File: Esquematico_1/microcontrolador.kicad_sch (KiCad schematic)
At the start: 31 parts, among them U2 STM32F405RGTx, Y1 Crystal

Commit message: Cristales y arreglo de los simbolos que no estaban en referencia
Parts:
- removed Y1: Crystal, symbol Device:Crystal
- added Y1: ABMM-8.000MHZ-D-4-T, ABMM25000MHZB2T, symbol ABMM-8_000MHZ-D-4-T:ABMM-8.000MHZ-D-4-T
- C5: value 10u -> 16pF
- C6: value C -> 16pF
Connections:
- net GND: now also C5.2, Y1.2 (METAL_LID_1), Y1.4 (METAL_LID_2); no longer C5.1
- net HSE_IN: now reaches U2.5 (PH0)
- net HSE_IN: now also C6.1, Y1.1 (X1); no longer C5.2
- net HSE_OUT: now reaches U2.6 (PH1)
- net HSE_OUT: now also C5.1, Y1.3 (X2); no longer C6.1
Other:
- moved on the sheet: C20, C21, C22, C23, C24, C25, C26, C27, C28, C29, C30, C31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

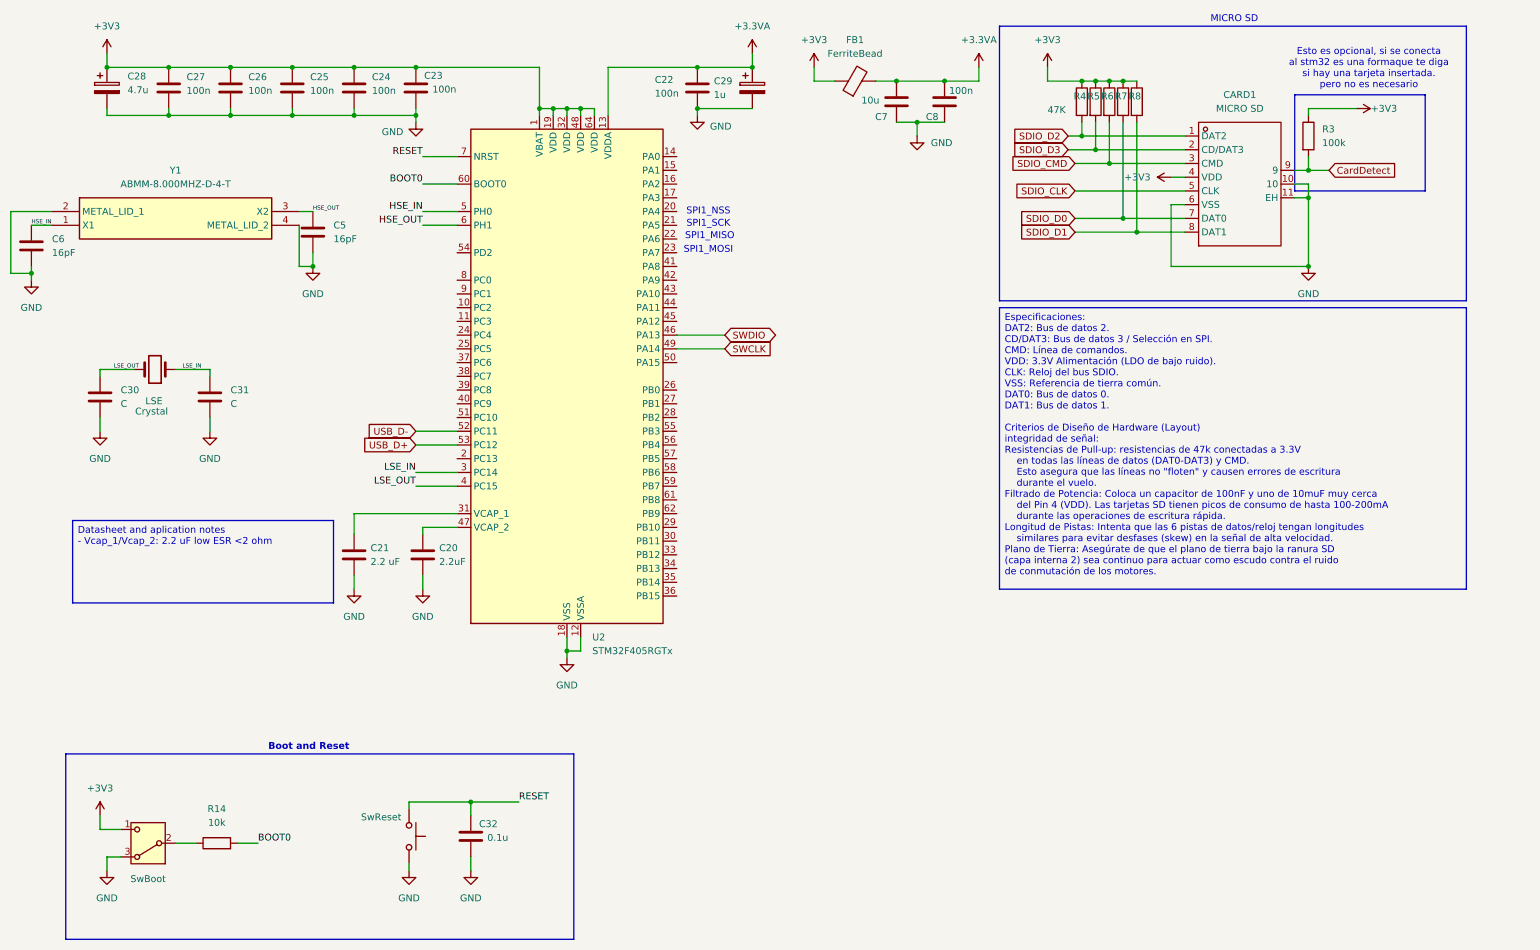
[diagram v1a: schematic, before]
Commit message: Conexiones con MCU, IMU, VTX, ELRS y  Magnometro
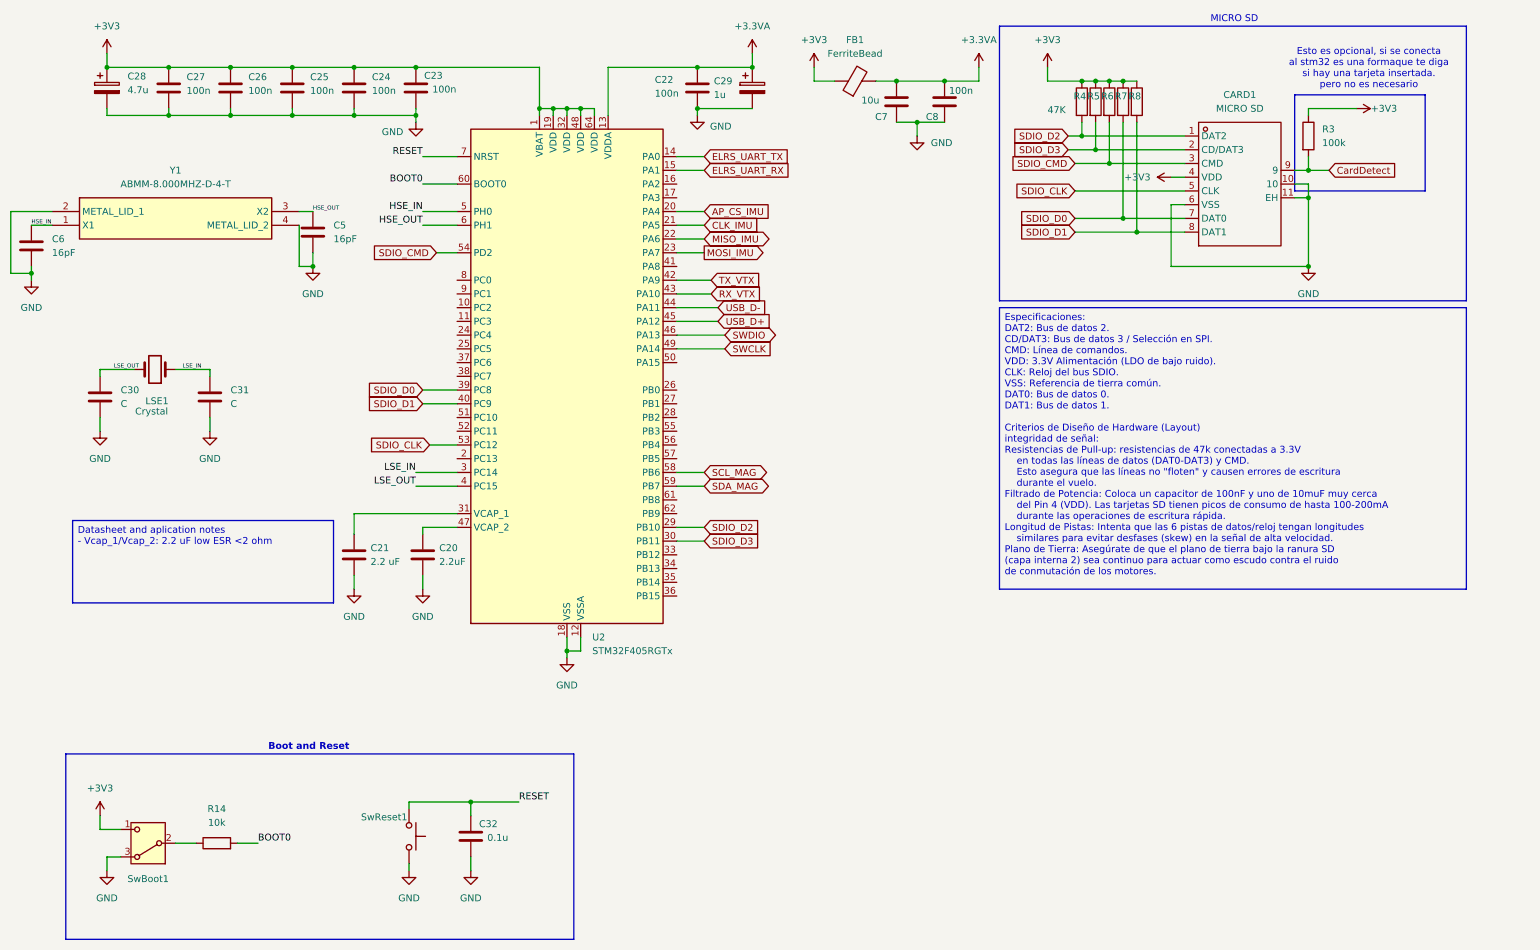
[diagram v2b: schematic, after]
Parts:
- Y1: footprint ABMM25000MHZB2T -> ABMM-8.000MHZ-D-4-T:ABMM25000MHZB2T
- renumbered LSE to LSE1, SwBoot to SwBoot1, SwReset to SwReset1
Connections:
- net SDIO_CLK: now also U2.53 (PC12)
- net SDIO_CMD: now also U2.54 (PD2)
- net SDIO_D0: now also U2.39 (PC8)
- net SDIO_D1: now also U2.40 (PC9)
- net SDIO_D2: now also U2.29 (PB10)
- net SDIO_D3: now also U2.30 (PB11)
- net USB_D+: now also U2.45 (PA12); no longer U2.53 (PC12)
- net USB_D-: now also U2.44 (PA11); no longer U2.52 (PC11)
- net ELRS_UART_TX: now reaches U2.14 (PA0)
- net ELRS_UART_RX: now reaches U2.15 (PA1)
- net AP_CS_IMU: now reaches U2.20 (PA4)
- net CLK_IMU: now reaches U2.21 (PA5)
- net MISO_IMU: now reaches U2.22 (PA6)
- net MOSI_IMU: now reaches U2.23 (PA7)
- net TX_VTX: now reaches U2.42 (PA9)
- net RX_VTX: now reaches U2.43 (PA10)
- net SCL_MAG: now reaches U2.58 (PB6)
- net SDA_MAG: now reaches U2.59 (PB7)
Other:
- note removed: "SPI1_MISO"
- note removed: "SPI1_MOSI"
- note removed: "SPI1_NSS"
- note removed: "SPI1_SCK"

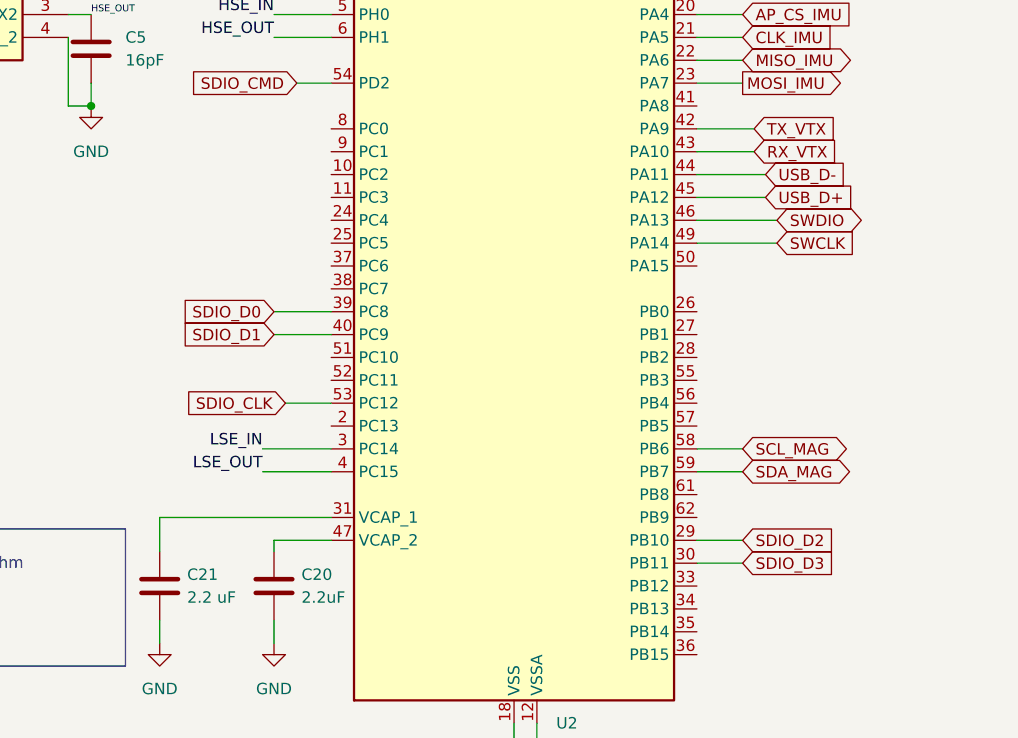
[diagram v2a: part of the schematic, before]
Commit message: último sensor conectado, y le quité los colores al net_signal xdd
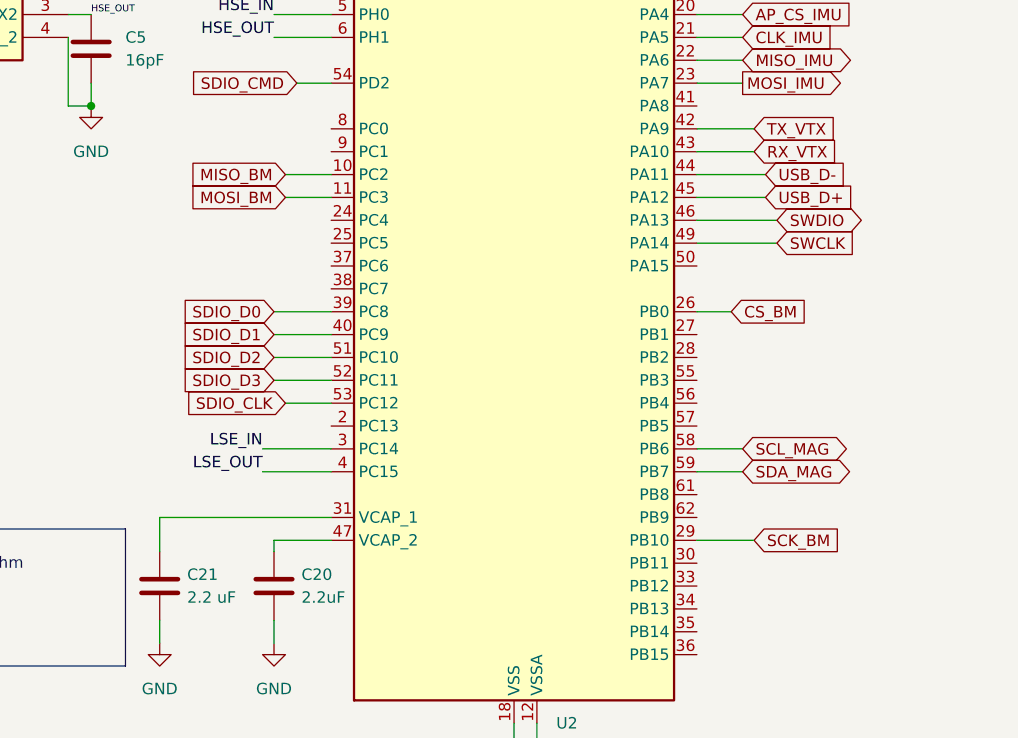
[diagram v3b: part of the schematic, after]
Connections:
- net SDIO_D2: now also U2.51 (PC10); no longer U2.29 (PB10)
- net SDIO_D3: now also U2.52 (PC11); no longer U2.30 (PB11)
- net MISO_BM: now reaches U2.10 (PC2)
- net MOSI_BM: now reaches U2.11 (PC3)
- net CS_BM: now reaches U2.26 (PB0)
- new net SCK_BM: U2.29 (PB10)
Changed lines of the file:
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@@
-	(wire
-		(pts
-			(xy 135.89 110.49) (xy 140.97 110.49)
-		)
-		(stroke
-			(width 0)
-			(type default)
-		)
-	)
 	(wire
 		(pts
@@
 	(wire
 		(pts
+			(xy 90.17 69.85) (xy 95.25 69.85)
+		)
+		(stroke
+			(width 0)
+			(type default)
+		)
+	)
+	(wire
+		(pts
+			(xy 95.25 90.17) (xy 88.9 90.17)
+		)
+		(stroke
+			(width 0)
+			(type default)
+		)
+	)
+	(wire
+		(pts
 			(xy 90.17 95.25) (xy 95.25 95.25)
 		)
@@
 	(wire
 		(pts
+			(xy 142.24 110.49) (xy 135.89 110.49)
+		)
+		(stroke
+			(width 0)
+			(type default)
+		)
+	)
+	(wire
+		(pts
 			(xy 135.89 77.47) (xy 144.78 77.47)
 		)
@@
 	(wire
 		(pts
+			(xy 88.9 92.71) (xy 95.25 92.71)
+		)
+		(stroke
+			(width 0)
+			(type default)
+		)
+	)
+	(wire
+		(pts
 			(xy 118.11 133.35) (xy 115.57 133.35)
 		)
@@
 	(wire
 		(pts
-			(xy 140.97 113.03) (xy 135.89 113.03)
-		)
-		(stroke
-			(width 0)
-			(type default)
-		)
-	)
-	(wire
-		(pts
 			(xy 53.34 25.4) (xy 64.77 25.4)
 		)
@@
 	(wire
 		(pts
+			(xy 90.17 72.39) (xy 95.25 72.39)
+		)
+		(stroke
+			(width 0)
+			(type default)
+		)
+	)
+	(wire
+		(pts
 			(xy 252.73 49.53) (xy 252.73 62.23)
 		)
@@
 		(pts
 			(xy 115.57 133.35) (xy 115.57 134.62)
+		)
+		(stroke
+			(width 0)
+			(type default)
+		)
+	)
+	(wire
+		(pts
+			(xy 139.7 85.09) (xy 135.89 85.09)
 		)
 		(stroke
@@
 			)
 			(justify right bottom)
+		)
+	)
+	(global_label "SCK_BM"
+		(shape input)
+		(at 142.24 110.49 0)
+		(fields_autoplaced yes)
+		(effects
+			(font
+				(size 1.27 1.27)
+			)
+			(justify left)
+		)
+		(property "Intersheetrefs" "${INTERSHEET_REFS}"
+			(at 152.6637 110.49 0)
+			(effects
+				(font
+					(size 1.27 1.27)
+				)
+				(justify left)
+				(hide yes)
+			)
 		)
 	)
@@
 		)
 	)
-	(global_label "SDIO_D2"
-		(shape input)
-		(at 140.97 110.49 0)
-		(fields_autoplaced yes)
-		(effects
-			(font
-				(size 1.27 1.27)
+	(global_label "TX_VTX"
+		(shape input)
+		(at 142.24 64.77 0)
+		(fields_autoplaced yes)
+		(effects
+			(font
+				(size 1.27 1.27)
+				(thickness 0.1588)
 			)
 			(justify left)
 		)
 		(property "Intersheetrefs" "${INTERSHEET_REFS}"
-			(at 151.8171 110.49 0)
+			(at 151.6356 64.77 0)
 			(effects
 				(font
@@
 		)
 	)
-	(global_label "TX_VTX"
-		(shape input)
-		(at 142.24 64.77 0)
-		(fields_autoplaced yes)
-		(effects
-			(font
-				(size 1.27 1.27)
-				(thickness 0.1588)
+	(global_label "SDIO_D0"
+		(shape input)
+		(at 88.9 85.09 180)
+		(fields_autoplaced yes)
+		(effects
+			(font
+				(size 1.27 1.27)
+			)
+			(justify right)
+		)
+		(property "Intersheetrefs" "${INTERSHEET_REFS}"
+			(at 78.0529 85.09 0)
+			(effects
+				(font
+					(size 1.27 1.27)
+				)
+				(justify right)
+				(hide yes)
+			)
+		)
+	)
+	(global_label "SDIO_D0"
+		(shape input)
+		(at 209.55 53.34 180)
+		(fields_autoplaced yes)
+		(effects
+			(font
+				(size 1.27 1.27)
+			)
+			(justify right)
+		)
+		(property "Intersheetrefs" "${INTERSHEET_REFS}"
+			(at 198.7029 53.34 0)
+			(effects
+				(font
+					(size 1.27 1.27)
+				)
+				(justify right)
+				(hide yes)
+			)
+		)
+	)
+	(global_label "AP_CS_IMU"
+		(shape input)
+		(at 140.97 52.07 0)
+		(fields_autoplaced yes)
+		(effects
+			(font
+				(size 1.27 1.27)
 			)
 			(justify left)
 		)
 		(property "Intersheetrefs" "${INTERSHEET_REFS}"
-			(at 151.6356 64.77 0)
+			(at 154.1152 52.07 0)
 			(effects
 				(font
@@
 		)
 	)
-	(global_label "SDIO_D0"
-		(shape input)
-		(at 88.9 85.09 180)
+	(global_label "SDIO_CMD"
+		(shape input)
+		(at 91.44 59.69 180)
 		(fields_autoplaced yes)
 		(effects
@@
 		)
 		(property "Intersheetrefs" "${INTERSHEET_REFS}"
-			(at 78.0529 85.09 0)
+			(at 79.081 59.69 0)
 			(effects
 				(font
@@
 		)
 	)
-	(global_label "SDIO_D0"
-		(shape input)
-		(at 209.55 53.34 180)
-		(fields_autoplaced yes)
-		(effects
-			(font
-				(size 1.27 1.27)
-			)
-			(justify right)
-		)
-		(property "Intersheetrefs" "${INTERSHEET_REFS}"
-			(at 198.7029 53.34 0)
-			(effects
-				(font
-					(size 1.27 1.27)
-				)
-				(justify right)
-				(hide yes)
-			)
-		)
-	)
-	(global_label "AP_CS_IMU"
-		(shape input)
-		(at 140.97 52.07 0)
+	(global_label "CS_BM"
+		(shape input)
+		(at 139.7 85.09 0)
 		(fields_autoplaced yes)
 		(effects
@@
 		)
 		(property "Intersheetrefs" "${INTERSHEET_REFS}"
-			(at 154.1152 52.07 0)
-			(effects
-				(font
-					(size 1.27 1.27)
-				)
-				(justify left)
-				(hide yes)
-			)
-		)
-	)
-	(global_label "SDIO_CMD"
-		(shape input)
-		(at 91.44 59.69 180)
-		(fields_autoplaced yes)
-		(effects
-			(font
-				(size 1.27 1.27)
-			)
-			(justify right)
-		)
-		(property "Intersheetrefs" "${INTERSHEET_REFS}"
-			(at 79.081 59.69 0)
-			(effects
-				(font
-					(size 1.27 1.27)
-				)
-				(justify right)
-				(hide yes)
-			)
-		)
-	)
-	(global_label "SDIO_D3"
-		(shape input)
-		(at 140.97 113.03 0)
-		(fields_autoplaced yes)
-		(effects
-			(font
-				(size 1.27 1.27)
-			)
-			(justify left)
-		)
-		(property "Intersheetrefs" "${INTERSHEET_REFS}"
-			(at 151.8171 113.03 0)
+			(at 148.8537 85.09 0)
 			(effects
 				(font
@@
 	(global_label "SDIO_D3"
 		(shape input)
+		(at 88.9 92.71 180)
+		(fields_autoplaced yes)
+		(effects
+			(font
+				(size 1.27 1.27)
+			)
+			(justify right)
+		)
+		(property "Intersheetrefs" "${INTERSHEET_REFS}"
+			(at 78.0529 92.71 0)
+			(effects
+				(font
+					(size 1.27 1.27)
+				)
+				(justify right)
+				(hide yes)
+			)
+		)
+	)
+	(global_label "SDIO_D3"
+		(shape input)
 		(at 208.28 40.64 180)
 		(fields_autoplaced yes)
@@
 		(property "Intersheetrefs" "${INTERSHEET_REFS}"
 			(at 78.0529 87.63 0)
+			(effects
+				(font
+					(size 1.27 1.27)
+				)
+				(justify right)
+				(hide yes)
+			)
+		)
+	)
+	(global_label "MOSI_BM"
+		(shape input)
+		(at 90.17 72.39 180)
+		(fields_autoplaced yes)
+		(effects
+			(font
+				(size 1.27 1.27)
+			)
+			(justify right)
+		)
+		(property "Intersheetrefs" "${INTERSHEET_REFS}"
+			(at 78.8996 72.39 0)
+			(effects
+				(font
+					(size 1.27 1.27)
+				)
+				(justify right)
+				(hide yes)
+			)
+		)
+	)
+	(global_label "MISO_BM"
+		(shape input)
+		(at 90.17 69.85 180)
+		(fields_autoplaced yes)
+		(effects
+			(font
+				(size 1.27 1.27)
+			)
+			(justify right)
+		)
+		(property "Intersheetrefs" "${INTERSHEET_REFS}"
+			(at 78.8996 69.85 0)
 			(effects
 				(font
@@
 				(hide yes)
 			)
+		)
+	)
+	(global_label "SDIO_D2"
+		(shape input)
+		(at 88.9 90.17 180)
+		(fields_autoplaced yes)
+		(effects
+			(font
+				(size 1.27 1.27)
+			)
+			(justify right)
+		)
+		(property "Intersheetrefs" "${INTERSHEET_REFS}"
+			(at 78.0529 90.17 0)
+			(effects
+				(font
+					(size 1.27 1.27)
+				)
+				(justify right)
+				(hide yes)
+			)

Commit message: Update llamada
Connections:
- net +3.3VA: no longer C7.2, C8.2, FB1.2
- new net +3V3A: C7.2, C8.2, FB1.2
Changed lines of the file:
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@@
 		(on_board yes)
 		(dnp no)
-		(fields_autoplaced yes)
 		(property "Reference" "#PWR031"
 			(at 191.77 29.21 0)
@@
 			)
 		)
-		(property "Value" "+3.3VA"
-			(at 191.77 20.32 0)
+		(property "Value" "+3V3A"
+			(at 188.214 21.336 0)
 			(effects
 				(font
 					(size 1.27 1.27)
 				)
+				(justify left)
 			)
 		)

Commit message: Update micro sd
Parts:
- added C34: 10u, symbol Device:C
- added C35: 100n, symbol Device:C
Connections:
- net +3V3: now also C34.2, C35.2
- net GND: now also C34.1, C35.1
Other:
- moved on the sheet: C30, C31, C5, C6, C7, C8, FB1, LSE1, Y1

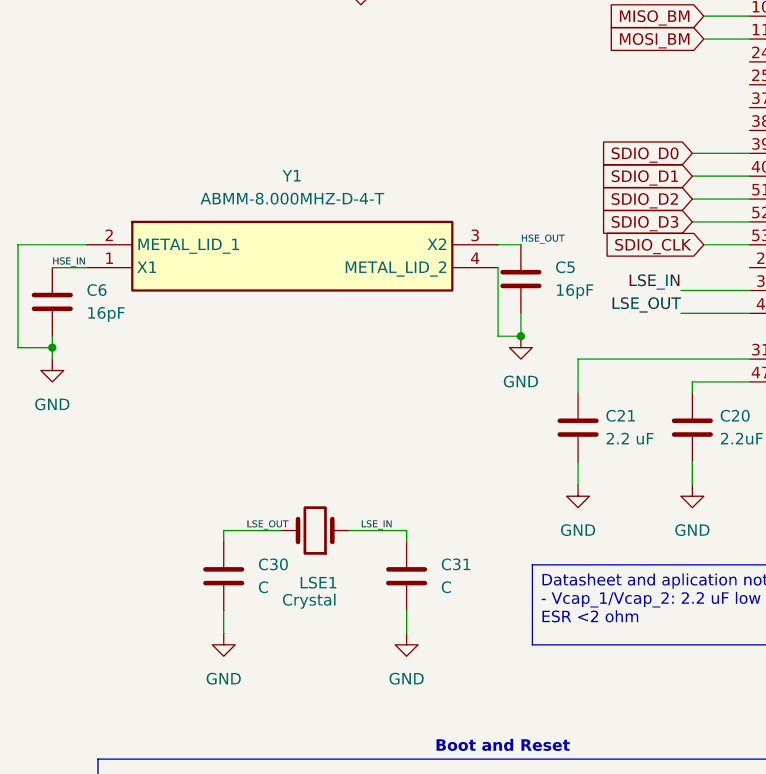
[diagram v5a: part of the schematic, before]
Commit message: Cambio del cristal por n-ésima vez
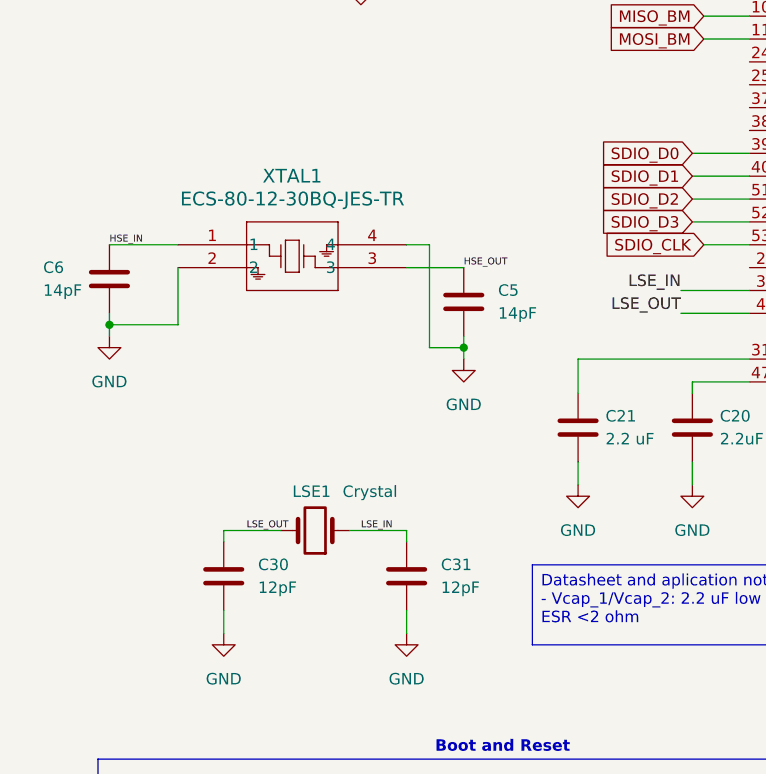
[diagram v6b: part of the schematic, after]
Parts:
- removed Y1: ABMM-8.000MHZ-D-4-T, ABMM-8.000MHZ-D-4-T:ABMM25000MHZB2T, symbol ABMM-8_000MHZ-D-4-T:ABMM-8.000MHZ-D-4-T
- added XTAL1: ECS-80-12-30BQ-JES-TR, ECS-80-12_ECS, symbol ESC8Mhz:ECS-80-12-30BQ-JES-TR
- C22, C23, C24, C25, C26, C27, C28, C29, C32, C34, C35, C7, C8: footprint (none) -> Capacitor_SMD:C_0805_2012Metric_Pad1.18x1.45mm_HandSolder
- C30, C31: value C -> 12pF
- C5, C6: value 16pF -> 14pF; footprint (none) -> Capacitor_SMD:C_0402_1005Metric_Pad0.74x0.62mm_HandSolder
- LSE1: footprint (none) -> ndx32khz:XTAL_NX3215SA_NDK
- R14, R4, R5, R6, R7, R8: footprint (none) -> Resistor_SMD:R_0805_2012Metric_Pad1.20x1.40mm_HandSolder
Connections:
- net GND: now also XTAL1.2, XTAL1.4
- net HSE_IN: now also XTAL1.1
- net HSE_OUT: now also XTAL1.3
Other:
- moved on the sheet: C5, C6
